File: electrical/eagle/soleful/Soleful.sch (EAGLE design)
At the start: 81 parts, among them IC1 STM32F405RGT, IC2 MCP1703DB, Q1 MOSFET, Q4 32.768kHz, SW1 RST, SW2 USR, U3 MIC2090-1YM5TR, Y1 12 MHz, Y2 32.768kHz

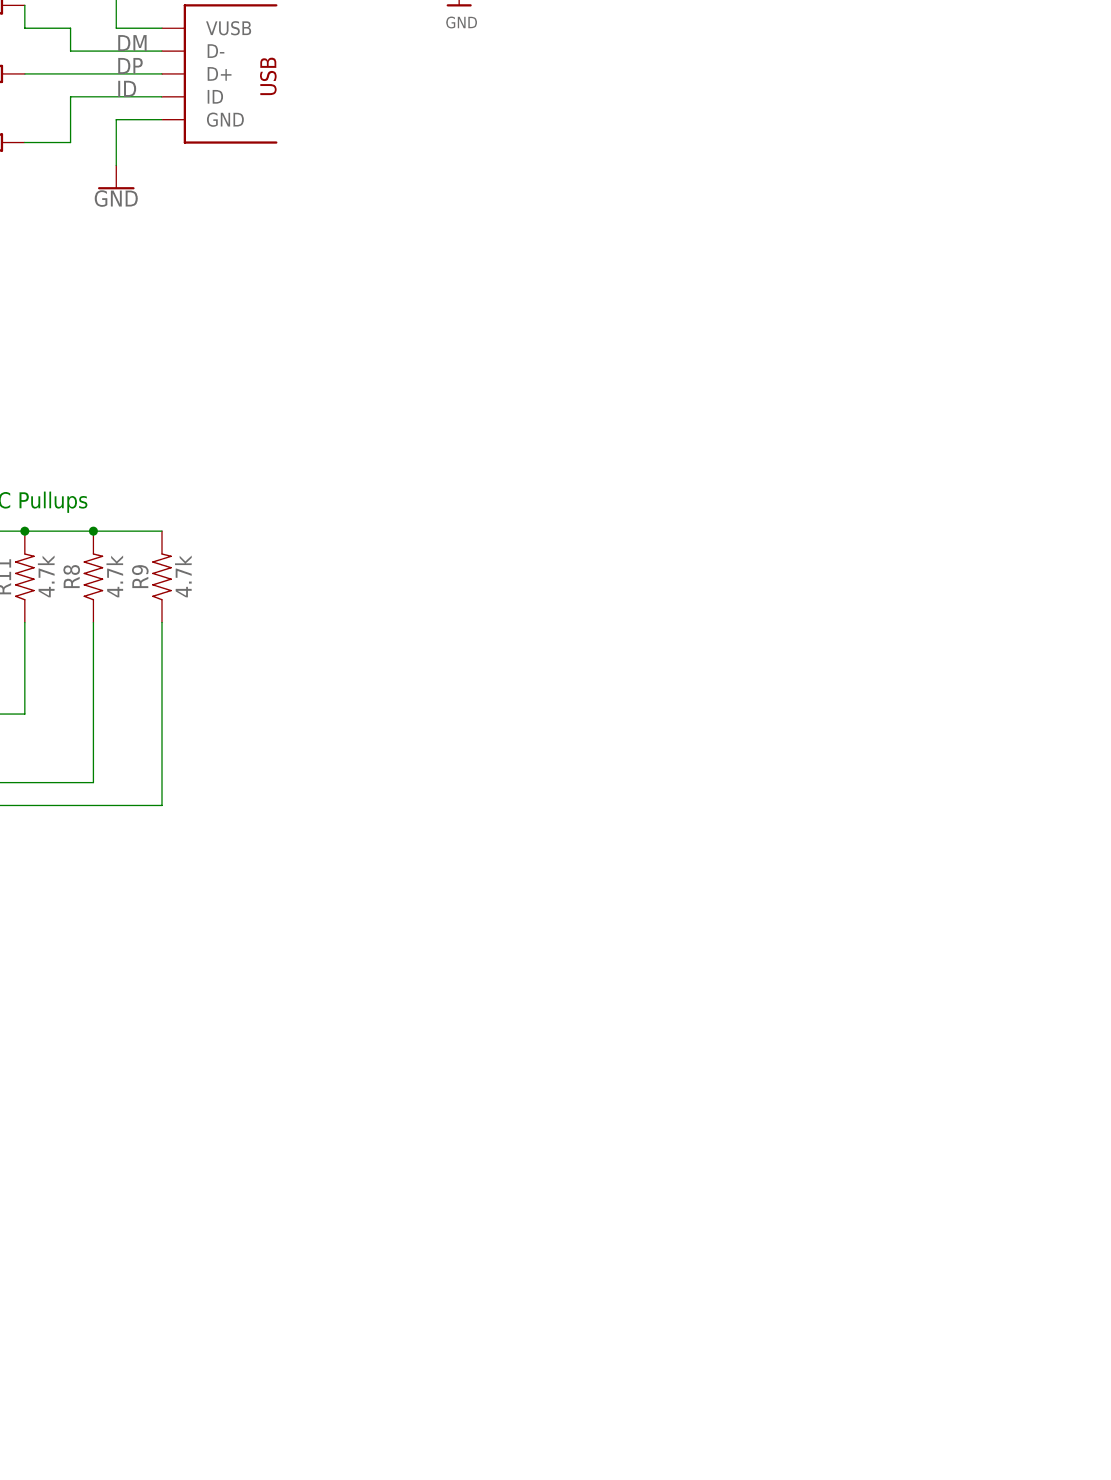
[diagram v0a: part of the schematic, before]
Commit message: Added LiPo charging IC, need to wire it together
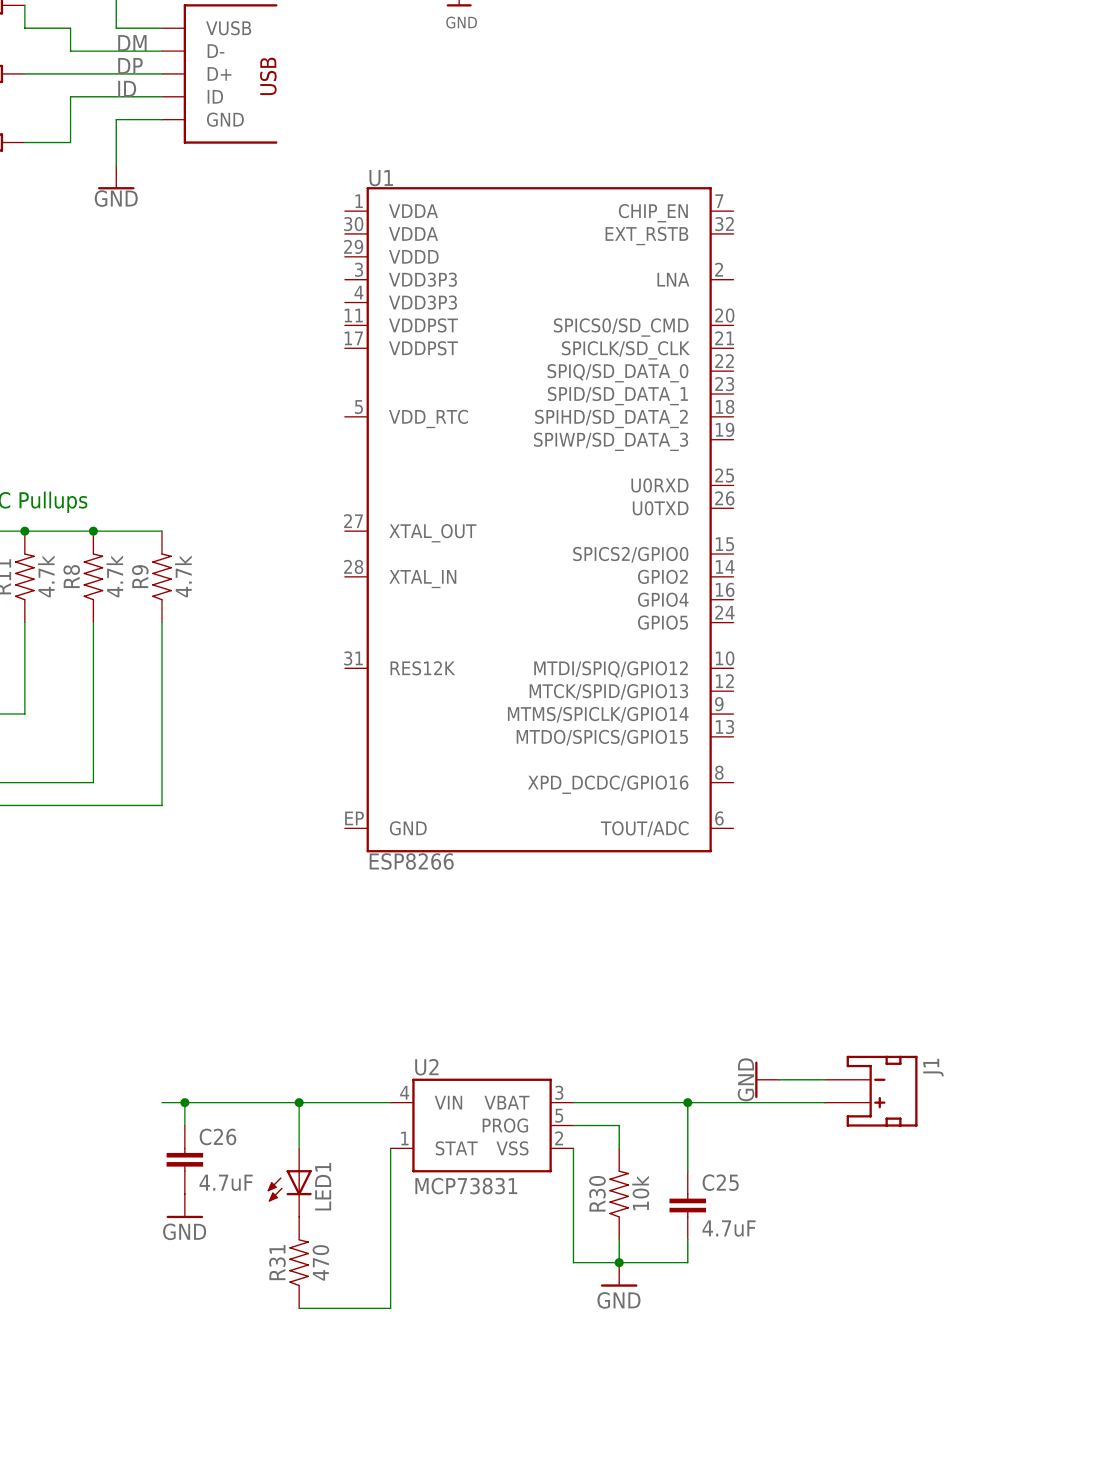
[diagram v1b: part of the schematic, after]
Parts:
- added C25, C26: 4.7uF, SparkFun-Capacitors:4.7UF-6.3V-10%(0603)
- added J1: (no value), SparkFun-Connectors:JST_2MM_MALE
- added LED1: (no value), SparkFun:LED3MM
- added R30: 10k, SparkFun-Resistors:10KOHM-0603-1/10W-1%
- added R31: 470, SparkFun-Resistors:470OHM-0603-1/10W-1%
- added U1: ESP8266, SparkFun-RF:ESP8266
- added U2: MCP73831, SparkFun-PowerIC:MCP73831
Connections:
- new net N$10: R30.2, U2.PROG
- new net N$14: C26.1, LED1.A, U2.VIN
- new net N$15: LED1.C, R31.2
- new net N$16: R31.1, U2.STAT
- new net N$9: C25.1, J1.+, U2.VBAT
- net GND: now also C25.2, C26.2, J1.-, R30.1, U2.VSS
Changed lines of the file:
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@@
 <part name="SUPPLY12" library="SparkFun-PowerSymbols" deviceset="VCC" device=""/>
 <part name="GND20" library="SparkFun-PowerSymbols" deviceset="GND" device=""/>
+<part name="U1" library="SparkFun-RF" deviceset="ESP8266" device=""/>
+<part name="U2" library="SparkFun-PowerIC" deviceset="MCP73831" device=""/>
+<part name="R30" library="SparkFun-Resistors" deviceset="10KOHM" device="-0603-1/10W-1%" value="10k"/>
+<part name="GND21" library="Icotech_Eagle_Library" deviceset="GND" device=""/>
+<part name="C25" library="SparkFun-Capacitors" deviceset="4.7UF-6.3V-10%(0603)" device="" value="4.7uF"/>
+<part name="J1" library="SparkFun-Connectors" deviceset="JST_2MM_MALE" device=""/>
+<part name="GND22" library="SparkFun-PowerSymbols" deviceset="GND" device=""/>
+<part name="LED1" library="SparkFun" deviceset="LED" device="3MM"/>
+<part name="R31" library="SparkFun-Resistors" deviceset="470OHM" device="-0603-1/10W-1%" value="470"/>
+<part name="C26" library="SparkFun-Capacitors" deviceset="4.7UF-6.3V-10%(0603)" device="" value="4.7uF"/>
+<part name="GND24" library="Icotech_Eagle_Library" deviceset="GND" device=""/>
 </parts>
 <sheets>
@@
 <instance part="SUPPLY12" gate="G$1" x="162.56" y="66.04"/>
 <instance part="GND20" gate="1" x="210.82" y="15.24"/>
+<instance part="U1" gate="G$1" x="274.32" y="157.48"/>
+<instance part="U2" gate="G$1" x="266.7" y="91.44"/>
+<instance part="R30" gate="G$1" x="281.94" y="83.82" rot="R90"/>
+<instance part="GND21" gate="1" x="281.94" y="73.66"/>
+<instance part="C25" gate="G$1" x="289.56" y="81.28"/>
+<instance part="J1" gate="G$1" x="309.88" y="96.52" rot="R270"/>
+<instance part="GND22" gate="1" x="297.18" y="96.52" rot="R270"/>
+<instance part="LED1" gate="G$1" x="246.38" y="86.36"/>
+<instance part="R31" gate="G$1" x="246.38" y="76.2" rot="R90"/>
+<instance part="C26" gate="G$1" x="233.68" y="86.36"/>
+<instance part="GND24" gate="1" x="233.68" y="81.28"/>
 </instances>
 <busses>
@@
 <junction x="205.74" y="53.34"/>
 </segment>
+<segment>
+<pinref part="R30" gate="G$1" pin="1"/>
+<wire x1="281.94" y1="78.74" x2="281.94" y2="76.2" width="0.1524" layer="91"/>
+<pinref part="GND21" gate="1" pin="GND"/>
+<pinref part="U2" gate="G$1" pin="VSS"/>
+<wire x1="276.86" y1="88.9" x2="276.86" y2="76.2" width="0.1524" layer="91"/>
+<wire x1="276.86" y1="76.2" x2="281.94" y2="76.2" width="0.1524" layer="91"/>
+<junction x="281.94" y="76.2"/>
+<pinref part="C25" gate="G$1" pin="2"/>
+<wire x1="289.56" y1="78.74" x2="289.56" y2="76.2" width="0.1524" layer="91"/>
+<wire x1="289.56" y1="76.2" x2="281.94" y2="76.2" width="0.1524" layer="91"/>
+</segment>
+<segment>
+<pinref part="J1" gate="G$1" pin="-"/>
+<wire x1="304.8" y1="96.52" x2="299.72" y2="96.52" width="0.1524" layer="91"/>
+<pinref part="GND22" gate="1" pin="GND"/>
+</segment>
+<segment>
+<pinref part="C26" gate="G$1" pin="2"/>
+<pinref part="GND24" gate="1" pin="GND"/>
+</segment>
 </net>
 <net name="N$1" class="0">
@@
 </segment>
 </net>
+<net name="N$9" class="0">
+<segment>
+<pinref part="U2" gate="G$1" pin="VBAT"/>
+<wire x1="276.86" y1="93.98" x2="289.56" y2="93.98" width="0.1524" layer="91"/>
+<wire x1="289.56" y1="93.98" x2="289.56" y2="86.36" width="0.1524" layer="91"/>
+<pinref part="C25" gate="G$1" pin="1"/>
+<wire x1="289.56" y1="93.98" x2="304.8" y2="93.98" width="0.1524" layer="91"/>
+<junction x="289.56" y="93.98"/>
+<pinref part="J1" gate="G$1" pin="+"/>
+</segment>
+</net>
+<net name="N$10" class="0">
+<segment>
+<pinref part="U2" gate="G$1" pin="PROG"/>
+<wire x1="276.86" y1="91.44" x2="281.94" y2="91.44" width="0.1524" layer="91"/>
+<wire x1="281.94" y1="91.44" x2="281.94" y2="88.9" width="0.1524" layer="91"/>
+<pinref part="R30" gate="G$1" pin="2"/>
+</segment>
+</net>
+<net name="N$14" class="0">
+<segment>
+<pinref part="U2" gate="G$1" pin="VIN"/>
+<wire x1="231.14" y1="93.98" x2="233.68" y2="93.98" width="0.1524" layer="91"/>
+<wire x1="233.68" y1="93.98" x2="246.38" y2="93.98" width="0.1524" layer="91"/>
+<wire x1="246.38" y1="93.98" x2="256.54" y2="93.98" width="0.1524" layer="91"/>
+<wire x1="246.38" y1="93.98" x2="246.38" y2="88.9" width="0.1524" layer="91"/>
+<junction x="246.38" y="93.98"/>
+<pinref part="LED1" gate="G$1" pin="A"/>
+<pinref part="C26" gate="G$1" pin="1"/>
+<wire x1="233.68" y1="91.44" x2="233.68" y2="93.98" width="0.1524" layer="91"/>
+<junction x="233.68" y="93.98"/>
+</segment>
+</net>
+<net name="N$15" class="0">
+<segment>
+<pinref part="LED1" gate="G$1" pin="C"/>
+<pinref part="R31" gate="G$1" pin="2"/>
+</segment>
+</net>
+<net name="N$16" class="0">
+<segment>
+<pinref part="R31" gate="G$1" pin="1"/>
+<pinref part="U2" gate="G$1" pin="STAT"/>
+<wire x1="246.38" y1="71.12" x2="256.54" y2="71.12" width="0.1524" layer="91"/>
+<wire x1="256.54" y1="71.12" x2="256.54" y2="88.9" width="0.1524" layer="91"/>
+</segment>
+</net>

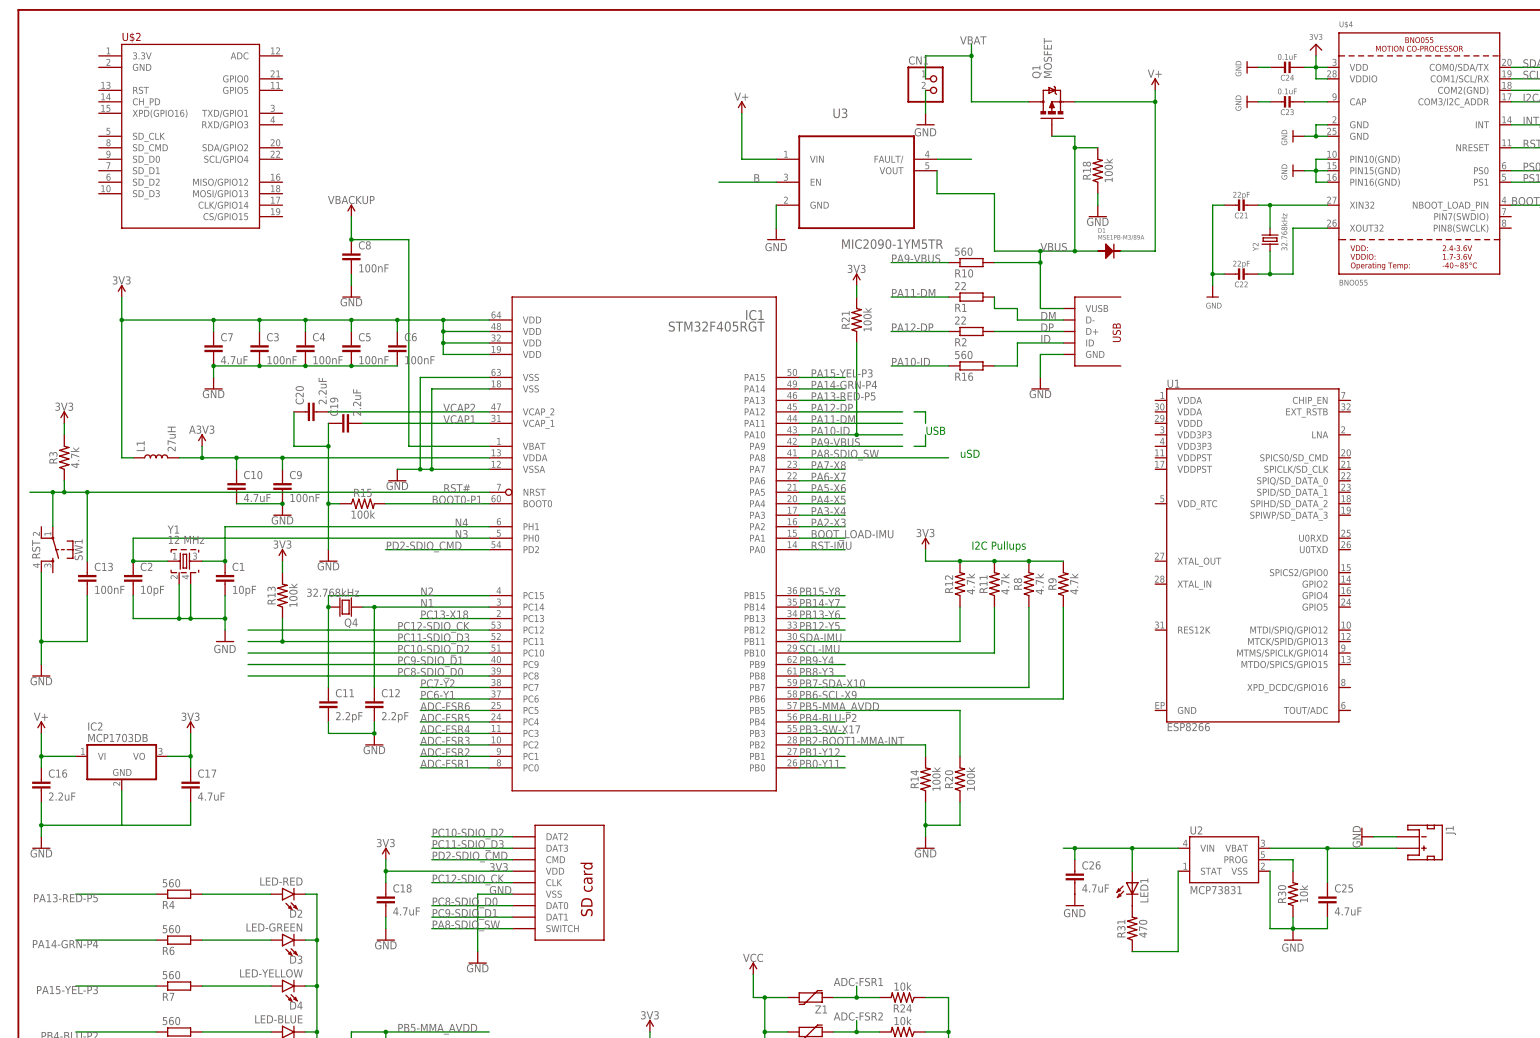
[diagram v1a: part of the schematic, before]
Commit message: Removed power switches and stuff until flow is determined
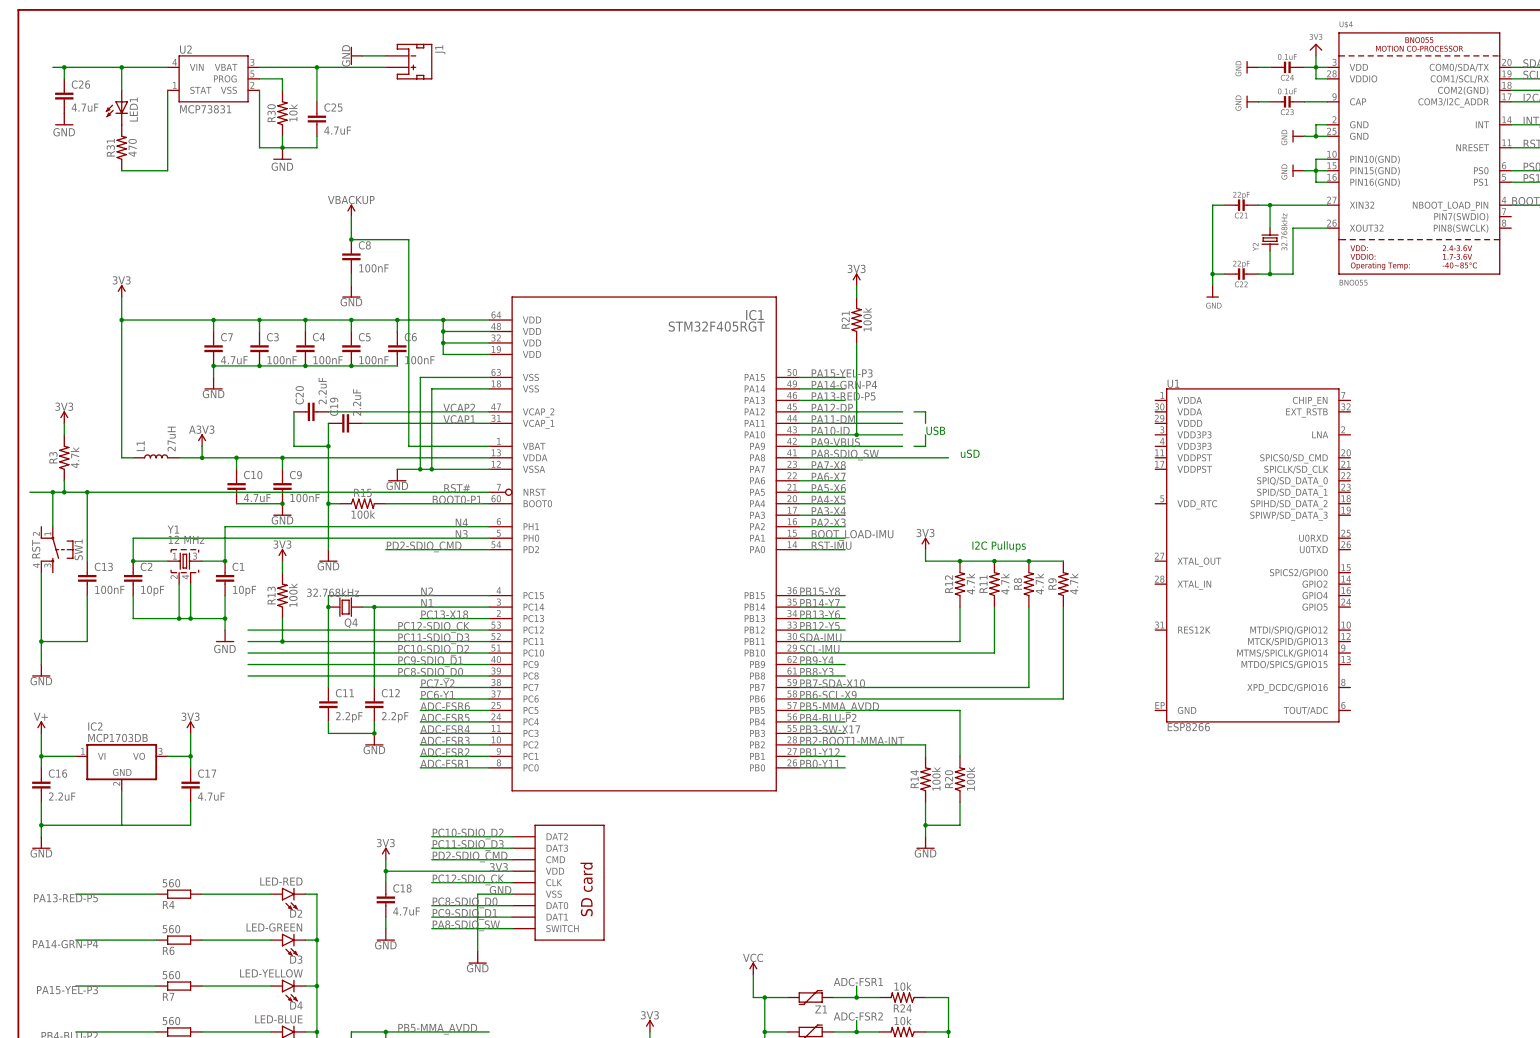
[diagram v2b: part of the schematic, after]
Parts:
- removed CN1: (no value), microbuilder:JST_2PIN
- removed D1: MSE1PB-M3/89A, PP_Passives:DIODE_MICROSMP
- removed Q1: MOSFET, User-Submitted:MOSFET-PCHANNEL
- removed R1, R2: 22, rcl:R-EU_R0603
- removed R10, R16: 560, rcl:R-EU_R0603
- removed R18: 100k, SparkFun-Resistors:100KOHM-0603-1/10W-1%
- removed U$10: USB-MICRO-AB, pyboard:USB-MICRO-AB
- removed U$2: (no value), esp8266modules:OLIMEX_MOD-WIFI-ESP8266-DEV>PINS-INSIDE
- removed U3: MIC2090-1YM5TR, Micrel_By_element14_Batch_1:MIC2090-1YM5TR
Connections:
- removed net B: U3.EN
- removed net DM: R1.2, U$10.D-
- removed net DP: R2.2, U$10.D+
- removed net ID: R16.2, U$10.ID
- removed net N$8: U3.FAULT/
- removed net VBAT: CN1.1, Q1.D
- removed net VBUS: D1.ANODE, Q1.G, R10.2, R18.2, U$10.VUSB, U3.VOUT
- net GND: no longer CN1.2, R18.1, U$10.GND, U3.GND
- net PA10-ID: no longer R16.1
- net PA11-DM: no longer R1.1
- net PA12-DP: no longer R2.1
- net PA9-VBUS: no longer R10.1
- net V+: no longer D1.CATHODE, Q1.S, U3.VIN
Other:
- moved on the sheet: C25, C26, J1, LED1, R30, R31, U2

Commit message: Some changes
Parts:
- removed U1: ESP8266, SparkFun-RF:ESP8266
- added X1: (no value), adafruit:ESP-12
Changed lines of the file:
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@@
 <part name="SUPPLY12" library="SparkFun-PowerSymbols" deviceset="VCC" device=""/>
 <part name="GND20" library="SparkFun-PowerSymbols" deviceset="GND" device=""/>
-<part name="U1" library="SparkFun-RF" deviceset="ESP8266" device=""/>
 <part name="U2" library="SparkFun-PowerIC" deviceset="MCP73831" device=""/>
 <part name="R30" library="SparkFun-Resistors" deviceset="10KOHM" device="-0603-1/10W-1%" value="10k"/>
@@
 <part name="C26" library="SparkFun-Capacitors" deviceset="4.7UF-6.3V-10%(0603)" device="" value="4.7uF"/>
 <part name="GND24" library="Icotech_Eagle_Library" deviceset="GND" device=""/>
+<part name="X1" library="adafruit" deviceset="ESP-12" device=""/>
 </parts>
 <sheets>
@@
 <instance part="SUPPLY12" gate="G$1" x="162.56" y="66.04"/>
 <instance part="GND20" gate="1" x="210.82" y="15.24"/>
-<instance part="U1" gate="G$1" x="274.32" y="157.48"/>
 <instance part="U2" gate="G$1" x="43.18" y="264.16"/>
 <instance part="R30" gate="G$1" x="58.42" y="256.54" rot="R90"/>
@@
 <instance part="C26" gate="G$1" x="10.16" y="259.08"/>
 <instance part="GND24" gate="1" x="10.16" y="254"/>
+<instance part="X1" gate="G$1" x="132.08" y="248.92"/>
 </instances>
 <busses>
